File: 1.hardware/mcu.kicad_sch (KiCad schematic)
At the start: 65 parts, among them IC3 STWD100NXWY3F, J3 Debug, Q1 PMOS, Q5 NMOS, Q6 NMOS, Q7 NMOS, SW2 SW_DPDT_x2, SW3 Reset_Btn, U1 STM32H743BITx, U15 TL431AIDBZR, X1 SMD3225-4, Y1 X161032768KGD2SI

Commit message: 핀 배치 완료
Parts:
- added Q11: NMOS, symbol Simulation_SPICE:NMOS
- added R114, R154: 2k/0.063w, Resistor_SMD:R_0402_1005Metric, symbol Device:R_Small_US
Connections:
- net 3V3_MCU: now also Q11.2 (G), R114.1
- net 5V: now also R154.1
- new net MOTOR_DIR: Q11.1 (D), R154.2
- new net MOTOR_DIR_INTR: Q11.3 (S), R114.2

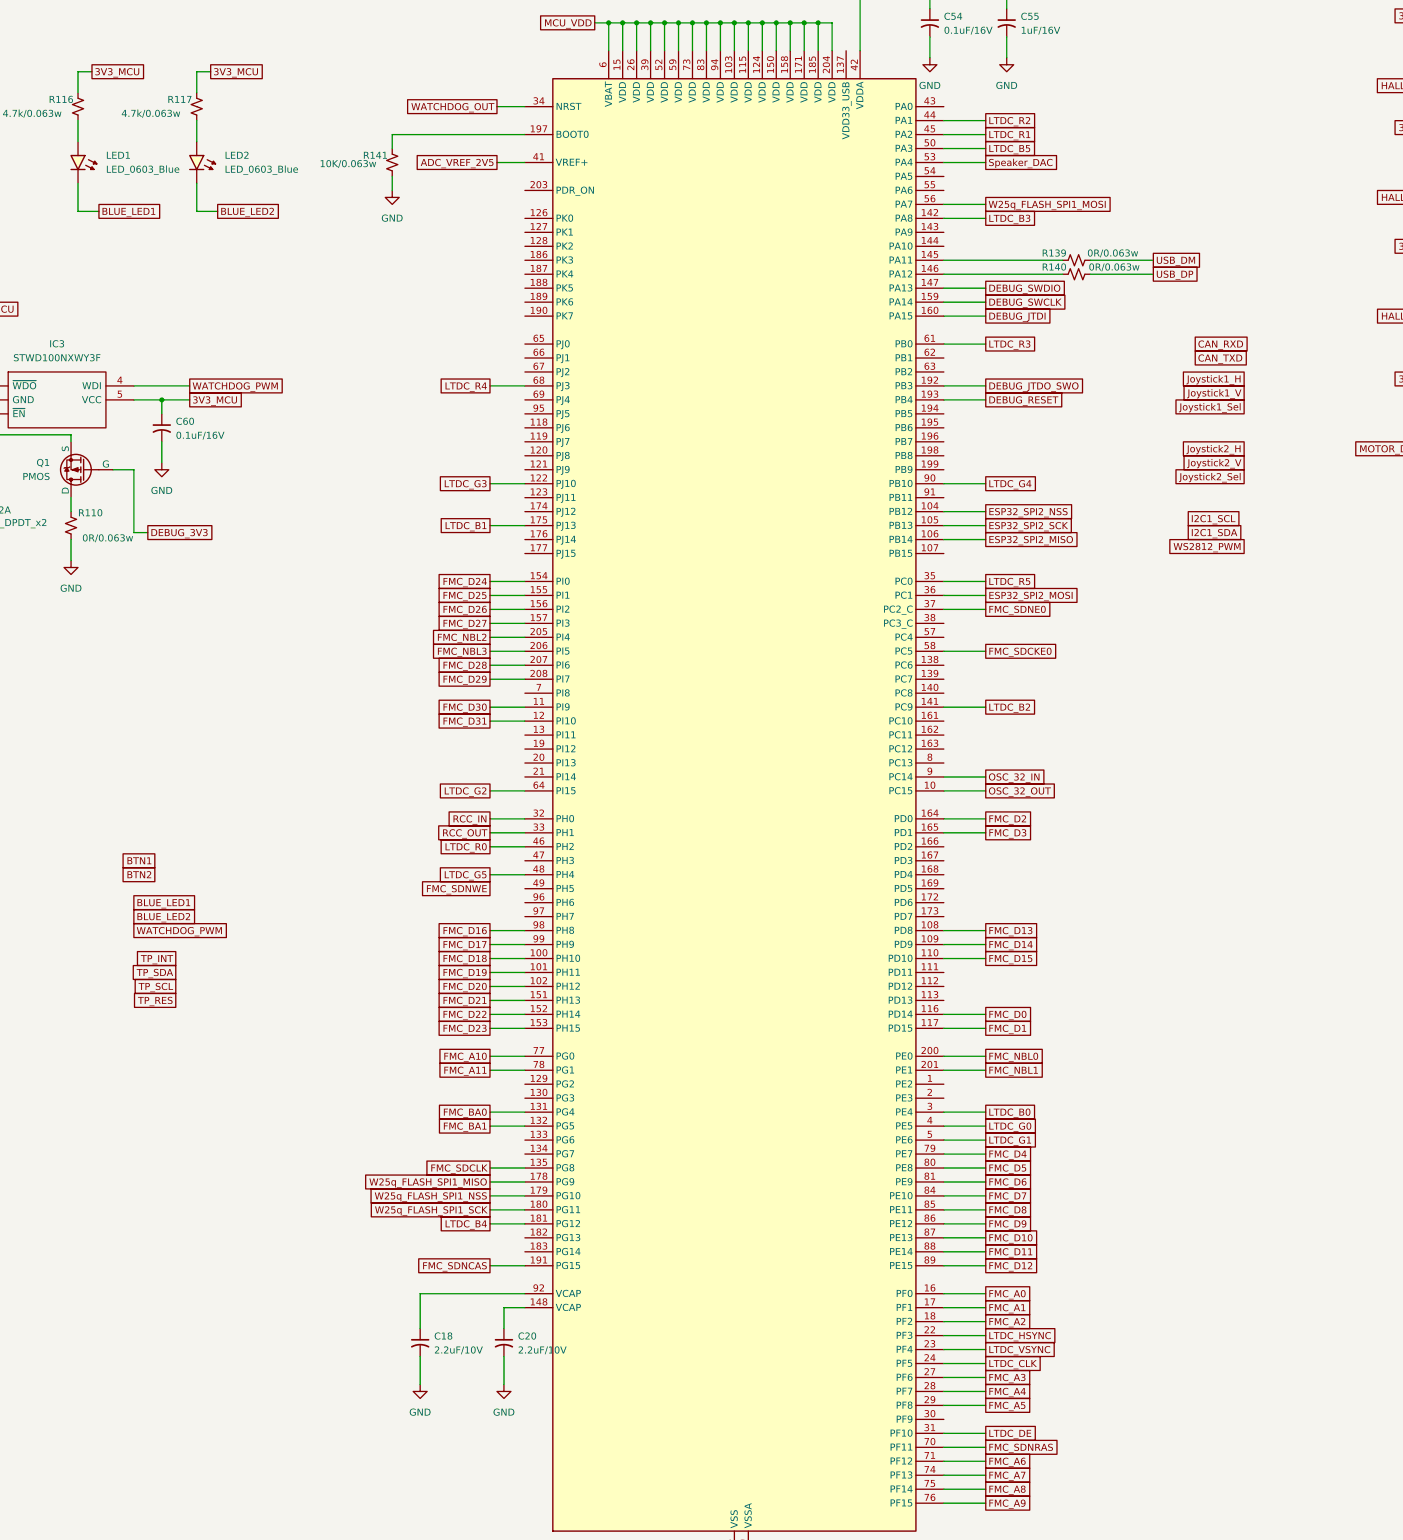
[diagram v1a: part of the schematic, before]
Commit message: 핀 배치 반영
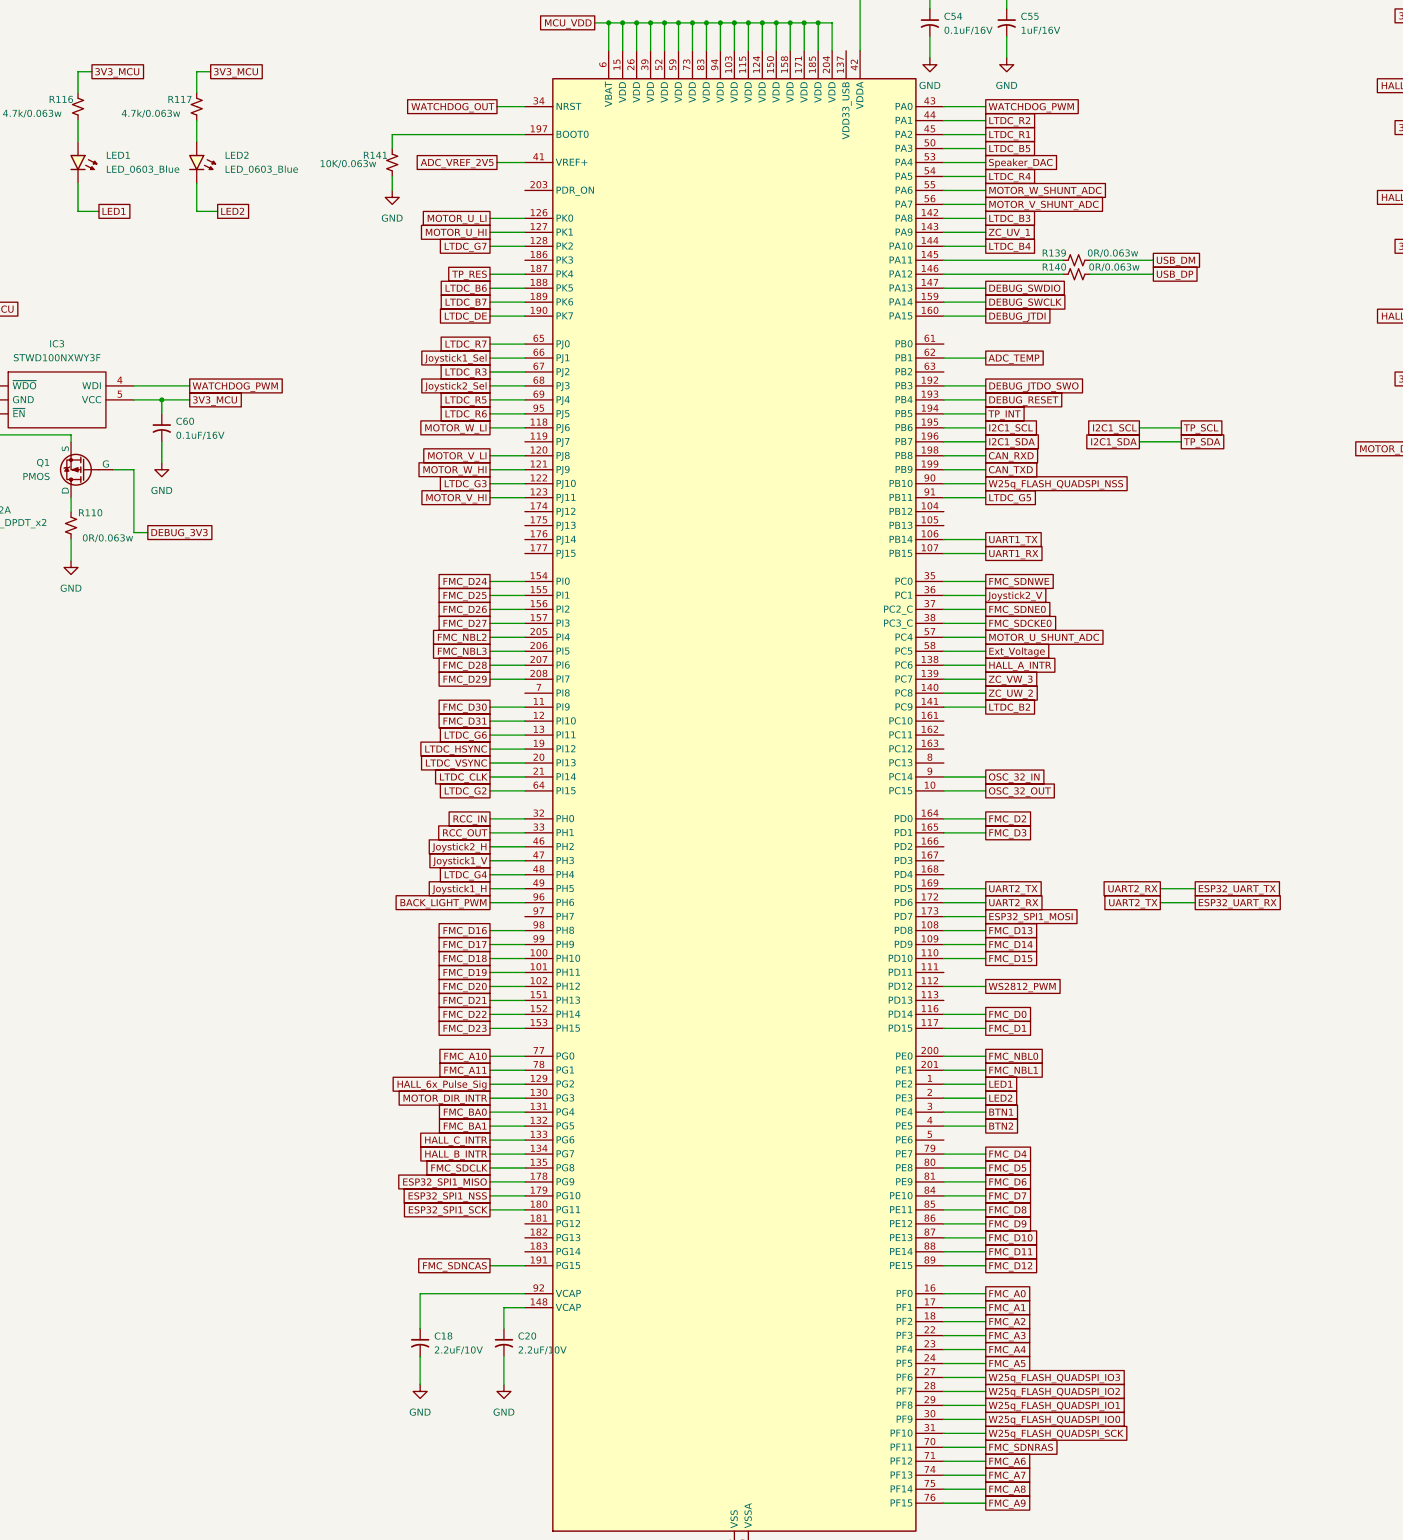
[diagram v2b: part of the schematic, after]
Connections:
- net BLUE_LED1 is gone; now on net LED1: LED1.1 (K)
- net BLUE_LED2 is gone; now on net LED2: LED2.1 (K)
- net ESP32_SPI2_MOSI is gone; now on net Joystick2_V: U1.36 (PC1)
- net LTDC_B0 is gone; now on net BTN1: U1.3 (PE4)
- net LTDC_G0 is gone; now on net BTN2: U1.4 (PE5)
- net LTDC_R0 is gone; now on net Joystick2_H: U1.46 (PH2)
- net CAN_RXD: now also U1.198 (PB8)
- net CAN_TXD: now also U1.199 (PB9)
- net FMC_A3: now also U1.22 (PF3); no longer U1.27 (PF6)
- net FMC_A4: now also U1.23 (PF4); no longer U1.28 (PF7)
- net FMC_A5: now also U1.24 (PF5); no longer U1.29 (PF8)
- net FMC_SDCKE0: now also U1.38 (PC3_C); no longer U1.58 (PC5)
- net FMC_SDNWE: now also U1.35 (PC0)
- net HALL_A_INTR: now also U1.138 (PC6)
- net HALL_B_INTR: now also U1.134 (PG7)
- net HALL_C_INTR: now also U1.133 (PG6)
- net I2C1_SCL: now also U1.195 (PB6)
- net I2C1_SDA: now also U1.196 (PB7)
- net Joystick1_H: now also U1.49 (PH5)
- net Joystick1_Sel: now also U1.66 (PJ1)
- net Joystick1_V: now also U1.47 (PH3)
- net Joystick2_Sel: now also U1.68 (PJ3)
- net LTDC_B4: now also U1.144 (PA10); no longer U1.181 (PG12)
- net LTDC_CLK: now also U1.21 (PI14); no longer U1.24 (PF5)
- net LTDC_DE: now also U1.190 (PK7); no longer U1.31 (PF10)
- net LTDC_G4: now also U1.48 (PH4); no longer U1.90 (PB10)
- net LTDC_G5: now also U1.91 (PB11); no longer U1.48 (PH4)
- net LTDC_HSYNC: now also U1.19 (PI12); no longer U1.22 (PF3)
- net LTDC_R3: now also U1.67 (PJ2); no longer U1.61 (PB0)
- net LTDC_R4: now also U1.54 (PA5); no longer U1.68 (PJ3)
- net LTDC_R5: now also U1.69 (PJ4); no longer U1.35 (PC0)
- net LTDC_VSYNC: now also U1.20 (PI13); no longer U1.23 (PF4)
- net MOTOR_DIR_INTR: now also U1.130 (PG3)
- net TP_INT: now also U1.194 (PB5)
- net TP_RES: now also U1.187 (PK4)
- net WATCHDOG_PWM: now also U1.43 (PA0)
- net WS2812_PWM: now also U1.112 (PD12)
- net LED1: now reaches U1.1 (PE2)
- net UART1_RX: now reaches U1.107 (PB15)
- net MOTOR_W_LI: now reaches U1.118 (PJ6)
- net MOTOR_V_LI: now reaches U1.120 (PJ8)
- net MOTOR_W_HI: now reaches U1.121 (PJ9)
- net MOTOR_V_HI: now reaches U1.123 (PJ11)
- net MOTOR_U_LI: now reaches U1.126 (PK0)
- net MOTOR_U_HI: now reaches U1.127 (PK1)
- net LTDC_G7: now reaches U1.128 (PK2)
- net HALL_6x_Pulse_Sig: now reaches U1.129 (PG2)
- net LTDC_G6: now reaches U1.13 (PI11)
- net ZC_VW_3: now reaches U1.139 (PC7)
- net ZC_UW_2: now reaches U1.140 (PC8)
- net ZC_UV_1: now reaches U1.143 (PA9)
- net ESP32_UART_RX: now reaches U1.169 (PD5)
- net ESP32_UART_TX: now reaches U1.172 (PD6)
- net ESP32_SPI1_MOSI: now reaches U1.173 (PD7)
- net LTDC_B6: now reaches U1.188 (PK5)
- net LTDC_B7: now reaches U1.189 (PK6)
- net LED2: now reaches U1.2 (PE3)
- net W25q_FLASH_QUADSPI_IO0: now reaches U1.30 (PF9)
- net MOTOR_W_SHUNT_ADC: now reaches U1.55 (PA6)
- net MOTOR_U_SHUNT_ADC: now reaches U1.57 (PC4)
- net ADC_TEMP: now reaches U1.62 (PB1)
- net LTDC_R7: now reaches U1.65 (PJ0)
- net LTDC_R6: now reaches U1.95 (PJ5)
- net BACK_LIGHT_PWM: now reaches U1.96 (PH6)
- net ESP32_SPI2_MISO renamed UART1_TX
- net ESP32_SPI2_NSS: no longer names the net of U1.104 (PB12)
- net ESP32_SPI2_SCK: no longer names the net of U1.105 (PB13)
- net LTDC_B1: no longer names the net of U1.175 (PJ13)
- net LTDC_G1: no longer names the net of U1.5 (PE6)
- net W25q_FLASH_SPI1_MISO renamed ESP32_SPI1_MISO
- net W25q_FLASH_SPI1_MOSI renamed MOTOR_V_SHUNT_ADC
- net W25q_FLASH_SPI1_NSS renamed ESP32_SPI1_NSS
- net W25q_FLASH_SPI1_SCK renamed ESP32_SPI1_SCK
- new net Ext_Voltage: U1.58 (PC5)
- new net W25q_FLASH_QUADSPI_IO1: U1.29 (PF8)
- new net W25q_FLASH_QUADSPI_IO2: U1.28 (PF7)
- new net W25q_FLASH_QUADSPI_IO3: U1.27 (PF6)
- new net W25q_FLASH_QUADSPI_NSS: U1.90 (PB10)
- new net W25q_FLASH_QUADSPI_SCK: U1.31 (PF10)

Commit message: 중간 저장
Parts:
- C29: renamed from C1; footprint (none) -> Capacitor_SMD:C_0603_1608Metric
- C30: renamed from C5; footprint (none) -> Capacitor_SMD:C_0402_1005Metric
- C32: renamed from C2; value 0.1uF/16V -> 0.1uF/50V; footprint (none) -> Capacitor_SMD:C_0603_1608Metric
- C34: renamed from C7; footprint (none) -> Capacitor_SMD:C_0402_1005Metric
- C35: renamed from C3; value 0.1uF/16V -> 0.1uF/50V; footprint (none) -> Capacitor_SMD:C_0603_1608Metric
- C36: renamed from C4; value 0.1uF/16V -> 0.1uF/50V; footprint (none) -> Capacitor_SMD:C_0603_1608Metric
- C37: renamed from C53; value 0.1uF/16V -> 0.1uF/50V; footprint (none) -> Capacitor_SMD:C_0603_1608Metric
- C38: renamed from C6; value 0.1uF/16V -> 0.1uF/50V; footprint (none) -> Capacitor_SMD:C_0603_1608Metric
- C39: renamed from C78; footprint (none) -> Capacitor_SMD:C_0603_1608Metric
- C40: renamed from C8; value 0.1uF/16V -> 0.1uF/50V; footprint (none) -> Capacitor_SMD:C_0603_1608Metric
- C41: renamed from C61; value 0.1uF/16V -> 0.1uF/50V; footprint (none) -> Capacitor_SMD:C_0603_1608Metric
- C42: renamed from C9; value 0.1uF/16V -> 0.1uF/50V; footprint (none) -> Capacitor_SMD:C_0603_1608Metric
- C43: renamed from C10; value 0.1uF/16V -> 0.1uF/50V; footprint (none) -> Capacitor_SMD:C_0603_1608Metric
- C44: renamed from C11; value 0.1uF/16V -> 0.1uF/50V; footprint (none) -> Capacitor_SMD:C_0603_1608Metric
- C45: renamed from C12; value 0.1uF/16V -> 0.1uF/50V; footprint (none) -> Capacitor_SMD:C_0603_1608Metric
- C46: renamed from C13; value 0.1uF/16V -> 0.1uF/50V; footprint (none) -> Capacitor_SMD:C_0603_1608Metric
- C47: renamed from C60; value 0.1uF/16V -> 0.1uF/50V; footprint (none) -> Capacitor_SMD:C_0603_1608Metric
- C48: renamed from C14; value 0.1uF/16V -> 0.1uF/50V; footprint (none) -> Capacitor_SMD:C_0603_1608Metric
- C49: renamed from C15; value 0.1uF/16V -> 0.1uF/50V; footprint (none) -> Capacitor_SMD:C_0603_1608Metric
- C50: renamed from C16; value 0.1uF/16V -> 0.1uF/50V; footprint (none) -> Capacitor_SMD:C_0603_1608Metric
- C51: renamed from C18; footprint (none) -> Capacitor_SMD:C_0603_1608Metric
- C52: renamed from C19; value 0.1uF/16V -> 0.1uF/50V; footprint (none) -> Capacitor_SMD:C_0603_1608Metric
- C53: renamed from C20; footprint (none) -> Capacitor_SMD:C_0603_1608Metric
- C54: renamed from C21; value 0.1uF/16V -> 0.1uF/50V; footprint (none) -> Capacitor_SMD:C_0603_1608Metric
- C55: renamed from C54; value 0.1uF/16V -> 0.1uF/50V; footprint (none) -> Capacitor_SMD:C_0603_1608Metric
- C56: renamed from C55; footprint (none) -> Capacitor_SMD:C_0603_1608Metric
- R16: renamed from R143; footprint (none) -> Resistor_SMD:R_0402_1005Metric
- R17: renamed from R144; footprint (none) -> Resistor_SMD:R_0402_1005Metric
- R26: renamed from R139; footprint (none) -> Resistor_SMD:R_0402_1005Metric
- R27: renamed from R140; footprint (none) -> Resistor_SMD:R_0402_1005Metric
- TP7: renamed from TP36; footprint (none) -> TestPoint:TestPoint_Pad_D1.5mm
- renumbered C68 to C31, C69 to C33, D10 to D8, IC3 to IC2, Q7 to Q2, Q6 to Q3, Q5 to Q4, Q11 to Q5, R111 to R15, R142 to R18, R96 to R19, R95 to R20, R94 to R21, R110 to R22, R116 to R23, R117 to R24, R141 to R25, R123 to R28, R121 to R29, R120 to R30, R114 to R31, R124 to R32, R122 to R33, R119 to R34, R154 to R35, S3 to S2, SW3 to SW2, SW2 to SW3, U15 to U1, U1 to U2
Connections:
- net GND: now also U2.203 (PDR_ON)
- no-connect marks 0 -> 25

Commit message: 중간 저장
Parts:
- removed D8: LL4148, PCM_Diode_SMD_AKL:D_MiniMELF, symbol PCM_Diode_AKL:LL4148
- added D8: B5819WS, SamacSys_Parts:SOD2613X100N, symbol SamacSys_Parts:B5819WS
- J3: value Debug -> DEBUG_CONN
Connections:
- net WATCHDOG_OUT: now also D8.2
- net at R20.1: now also D8.1
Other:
- moved on the sheet: C41, R20, SW2

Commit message: 풋프린트 연결 완료
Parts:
- removed D8: B5819WS, SamacSys_Parts:SOD2613X100N, symbol SamacSys_Parts:B5819WS
- removed IC2: STWD100NXWY3F, SamacSys_Parts:SOT95P280X145-5N, symbol SamacSys_Parts:STWD100NXWY3F
- removed Q1: PMOS, symbol Simulation_SPICE:PMOS
- removed Q2, Q3, Q4, Q5: NMOS, symbol Simulation_SPICE:NMOS
- removed R19: 10k/0.063w, Resistor_SMD:R_0402_1005Metric, symbol Device:R_Small_US
- removed R20: 100/0.063w, Resistor_SMD:R_0402_1005Metric, symbol Device:R_Small_US
- removed R21: 4.7k/0.063w, Resistor_SMD:R_0402_1005Metric, symbol Device:R_Small_US
- removed R22: 0R/0.063w, Resistor_SMD:R_0402_1005Metric, symbol Device:R_Small_US
- removed R28, R29, R30, R31, R32, R33, R34, R35: 2k/0.063w, Resistor_SMD:R_0402_1005Metric, symbol Device:R_Small_US
- removed SW2: Reset_Btn, symbol Switch:SW_Push
- removed SW3: SW_DPDT_x2, symbol Switch:SW_DPDT_x2
- added C125: 0.1uF/50V, Capacitor_SMD:C_0603_1608Metric, symbol Device:C_Small_US
- added S4: TSB008A2518A, SamacSys_Parts_Project:TSB008A2518A, symbol SamacSys_Parts:TSB008A2518A
- added U11: TXS0104EPW, Package_SO:TSSOP-14_4.4x5mm_P0.65mm, symbol Logic_LevelTranslator:TXS0104EPW
- J3: footprint (none) -> Connector_PinSocket_2.54mm:PinSocket_1x07_P2.54mm_Vertical
- S1, S2: footprint SamacSys_Parts:TSB008A2518A -> SamacSys_Parts_Project:TSB008A2518A
- U1: footprint SamacSys_Parts:SOT95P237X112-3N -> SamacSys_Parts_Project:SOT95P237X112-3N
- Y1: value X161032768KGD2SI -> X1A0000610002; footprint (none) -> Crystal:Crystal_SMD_2012-2Pin_2.0x1.2mm
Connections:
- net 3V3_MCU: now also U11.1 (V_{CCA})
- net 5V: now also C125.1, U11.14 (V_{CCB})
- net GND: now also C125.2, S4.1 (COM), U11.7 (GND)
- net HALL_A: now also U11.13 (B1)
- net HALL_A_INTR: now also U11.2 (A1)
- net HALL_B: now also U11.12 (B2)
- net HALL_B_INTR: now also U11.3 (A2)
- net HALL_C: now also U11.11 (B3)
- net HALL_C_INTR: now also U11.4 (A3)
- net MOTOR_DIR: now also U11.10 (B4)
- net MOTOR_DIR_INTR: now also U11.5 (A4)
- net OE_PIN: now reaches U2.119 (PJ7)
- net OE_PIN: now also U11.8 (OE)
- net WATCHDOG_OUT: no longer names the net of C41.1, U2.34 (NRST)
- net WATCHDOG_OUT: now also S4.2 (NO)
- net WATCHDOG_PWM: no longer names the net of U2.43 (PA0)
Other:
- moved on the sheet: C37, C39, J3, LED1, LED2, R15, R18, R23, R24, TP7, U1

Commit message: 중간 저장
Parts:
- renumbered C29 to C30, C30 to C31, C31 to C32, C32 to C33, C33 to C34, C34 to C35, C35 to C36, C36 to C37, C40 to C39, C37 to C40, C39 to C41, C48 to C47, C41 to C48, C47 to C57, C125 to C58, R16 to R15, R15 to R16, R23 to R18, R24 to R19, R18 to R20, R25 to R21, R26 to R22, R27 to R23, S1 to S2, S2 to S3, U11 to U3
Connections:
- net EXTRA_SPI3_SCK: now reaches U2.161 (PC10)
- net EXTRA_SPI3_MISO: now reaches U2.162 (PC11)
- net EXTRA_SPI3_MOSI: now reaches U2.163 (PC12)
- net EXTRA_SPI3_NSS: now reaches U2.166 (PD2)
- net Joystick1_H renamed Joystick_H
- net Joystick1_Sel renamed Joystick_Sel
- net Joystick1_V renamed Joystick_V
- net Joystick2_H: no longer names the net of U2.46 (PH2)
- net Joystick2_Sel: no longer names the net of U2.68 (PJ3)
- net Joystick2_V: no longer names the net of U2.36 (PC1)
- no-connect marks 25 -> 22

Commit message: 중간 저장
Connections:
- net GND: now also S4.2 (NO); no longer S4.1 (COM)
- net at C48.1, U2.34 (NRST): now also S4.1 (COM); no longer S4.2 (NO)
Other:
- moved on the sheet: S4
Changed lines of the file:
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@@
 	)
 	(junction
+		(at 190.5 97.79)
+		(diameter 0)
+		(color 0 0 0 0)
+	)
+	(junction
 		(at 262.89 66.04)
 		(diameter 0)
@@
 	)
 	(junction
-		(at 190.5 97.79)
-		(diameter 0)
-		(color 0 0 0 0)
-	)
-	(junction
 		(at 273.05 66.04)
 		(diameter 0)
@@
 	(wire
 		(pts
-			(xy 190.5 81.28) (xy 190.5 88.9)
-		)
-		(stroke
-			(width 0)
-			(type default)
-		)
-	)
-	(wire
-		(pts
 			(xy 100.33 119.38) (xy 97.79 119.38)
 		)
@@
 	(wire
 		(pts
-			(xy 190.5 91.44) (xy 190.5 97.79)
-		)
-		(stroke
-			(width 0)
-			(type default)
-		)
-	)
-	(wire
-		(pts
 			(xy 151.13 35.56) (xy 137.16 35.56)
 		)
@@
 	(wire
 		(pts
+			(xy 190.5 81.28) (xy 190.5 90.17)
+		)
+		(stroke
+			(width 0)
+			(type default)
+		)
+	)
+	(wire
+		(pts
 			(xy 245.11 297.18) (xy 226.06 297.18)
 		)
@@
 	(wire
 		(pts
+			(xy 190.5 92.71) (xy 190.5 97.79)
+		)
+		(stroke
+			(width 0)
+			(type default)
+		)
+	)
+	(wire
+		(pts
 			(xy 238.76 256.54) (xy 245.11 256.54)
 		)
@@
 	(symbol
 		(lib_id "SamacSys_Parts:TSB008A2518A")
-		(at 190.5 91.44 180)
+		(at 190.5 90.17 0)
+		(mirror y)
 		(unit 1)
 		(exclude_from_sim no)
@@
 		(on_board yes)
 		(dnp no)
-		(fields_autoplaced yes)
 		(property "Reference" "S4"
-			(at 179.07 81.28 0)
+			(at 179.07 100.33 0)
 			(effects
 				(font
@@
 		)
 		(property "Value" "TSB008A2518A"
-			(at 179.07 83.82 0)
+			(at 179.07 97.79 0)
 			(effects
 				(font
@@
 		)
 		(property "Footprint" "SamacSys_Parts_Project:TSB008A2518A"
-			(at 171.45 93.98 0)
+			(at 171.45 87.63 0)
 			(effects
 				(font
@@
 		)
 		(property "Datasheet" "https://datasheet.lcsc.com/lcsc/2108261830_BZCN-TSB008A2518A_C2888455.pdf"
-			(at 171.45 91.44 0)
+			(at 171.45 90.17 0)
 			(effects
 				(font
@@
 		)
 		(property "Description" "3.5mm 2.5mm Rectangle button 50mA Brick nogging 6mm 180gf 12V SMD Tactile Switches ROHS"
-			(at 190.5 91.44 0)
+			(at 190.5 90.17 0)
 			(effects
 				(font
@@
 		)
 		(property "Description_1" "3.5mm 2.5mm Rectangle button 50mA Brick nogging 6mm 180gf 12V SMD Tactile Switches ROHS"
-			(at 171.45 88.9 0)
+			(at 171.45 92.71 0)
 			(effects
 				(font
@@
 		)
 		(property "Height" "2.75"
-			(at 171.45 86.36 0)
+			(at 171.45 95.25 0)
 			(effects
 				(font
@@
 		)
 		(property "Manufacturer_Name" "BZCN"
-			(at 171.45 83.82 0)
+			(at 171.45 97.79 0)
 			(effects
 				(font
@@
 		)
 		(property "Manufacturer_Part_Number" "TSB008A2518A"
-			(at 171.45 81.28 0)
+			(at 171.45 100.33 0)
 			(effects
 				(font
@@
 		)
 		(property "Mouser Part Number" ""
-			(at 171.45 78.74 0)
+			(at 171.45 102.87 0)
 			(effects
 				(font
@@
 		)
 		(property "Mouser Price/Stock" ""
-			(at 171.45 76.2 0)
+			(at 171.45 105.41 0)
 			(effects
 				(font
@@
 		)
 		(property "Arrow Part Number" ""
-			(at 171.45 73.66 0)
+			(at 171.45 107.95 0)
 			(effects
 				(font
@@
 		)
 		(property "Arrow Price/Stock" ""
-			(at 171.45 71.12 0)
+			(at 171.45 110.49 0)
 			(effects
 				(font
